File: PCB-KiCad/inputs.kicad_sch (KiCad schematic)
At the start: 39 parts, among them SW1 SW_DPDT_x2, SW2 SW_DPDT_x2, SW3 SW_DPDT_x2, SW4 SW_DPDT_x2, SW5 SW_DPDT_x2, U5 ATtiny84A-P, U6 74HC165, U7 74HC165

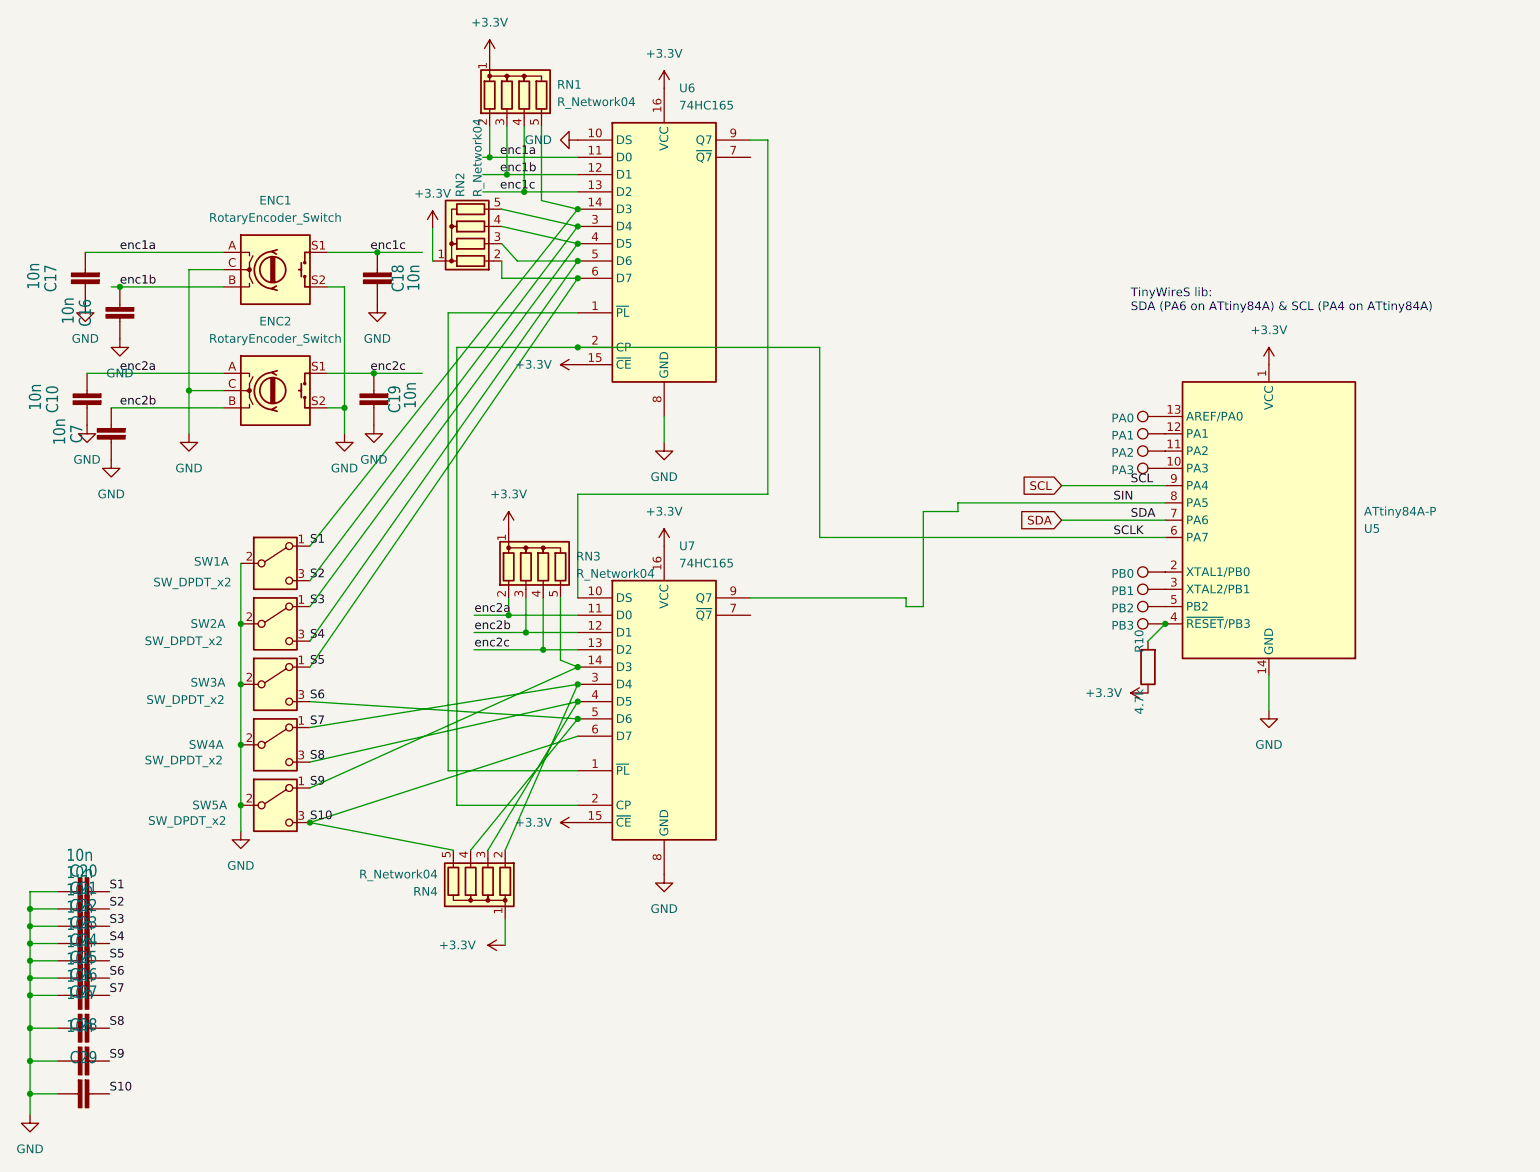
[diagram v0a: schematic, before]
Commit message: GP1291 fixes, removed input mcu, added SRCs.
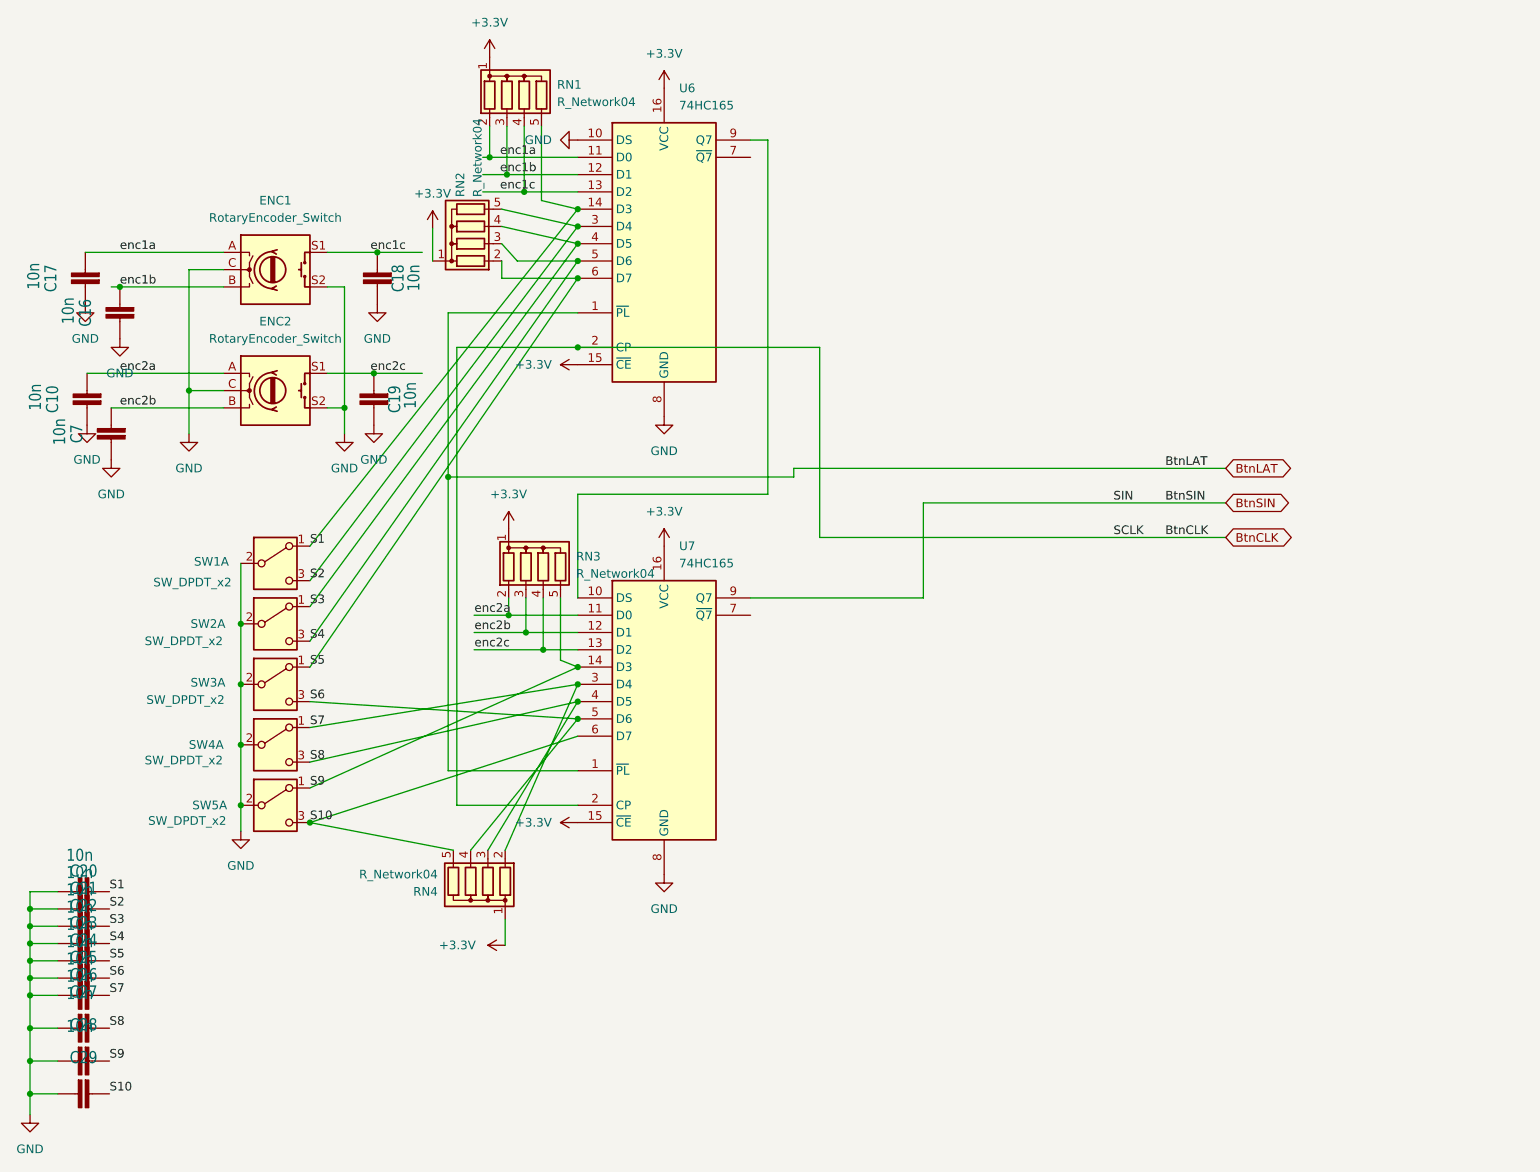
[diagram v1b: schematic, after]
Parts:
- removed PA0: PA0, TestPoint:TestPoint_Pad_2.0x2.0mm, symbol Connector:TestPoint
- removed PA1: PA1, TestPoint:TestPoint_Pad_2.0x2.0mm, symbol Connector:TestPoint
- removed PA2: PA2, TestPoint:TestPoint_Pad_2.0x2.0mm, symbol Connector:TestPoint
- removed PA3: PA3, TestPoint:TestPoint_Pad_2.0x2.0mm, symbol Connector:TestPoint
- removed PB0: PB0, TestPoint:TestPoint_Pad_2.0x2.0mm, symbol Connector:TestPoint
- removed PB1: PB1, TestPoint:TestPoint_Pad_2.0x2.0mm, symbol Connector:TestPoint
- removed PB2: PB2, TestPoint:TestPoint_Pad_2.0x2.0mm, symbol Connector:TestPoint
- removed PB3: PB3, TestPoint:TestPoint_Pad_2.0x2.0mm, symbol Connector:TestPoint
- removed R10: 4.7k, Resistor_SMD:R_1206_3216Metric_Pad1.30x1.75mm_HandSolder, symbol Device:R
- removed U5: ATtiny84A-P, Package_DIP:DIP-14_W7.62mm, symbol MCU_Microchip_ATtiny:ATtiny84A-P
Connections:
- net BtnLAT: now reaches U6.1 (~{PL}), U7.1 (~{PL})
- net SCLK renamed BtnCLK
- net SIN renamed BtnSIN
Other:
- note removed: "TinyWireS lib: SDA (PA6 on ATtiny84A) & SCL (PA4 on ATtiny84A)"
